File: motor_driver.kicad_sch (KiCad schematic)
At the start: 8 parts, among them J3 Conn_01x06, J4 Conn_01x06, U10 TB6612FNG

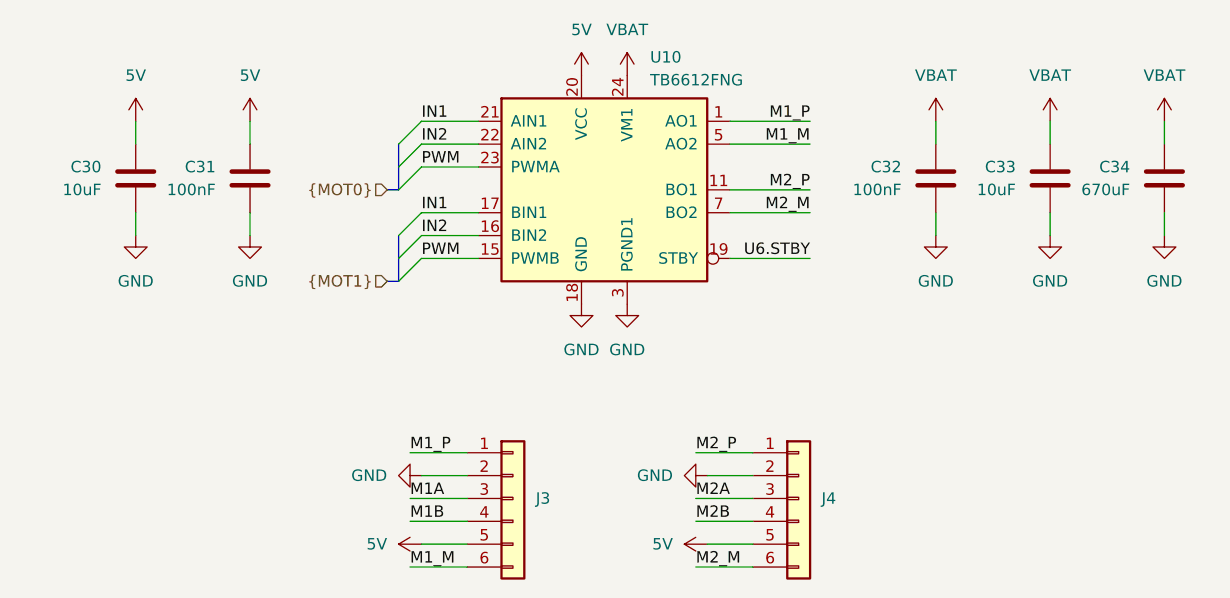
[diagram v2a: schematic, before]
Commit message: Follow DC-DC typical application
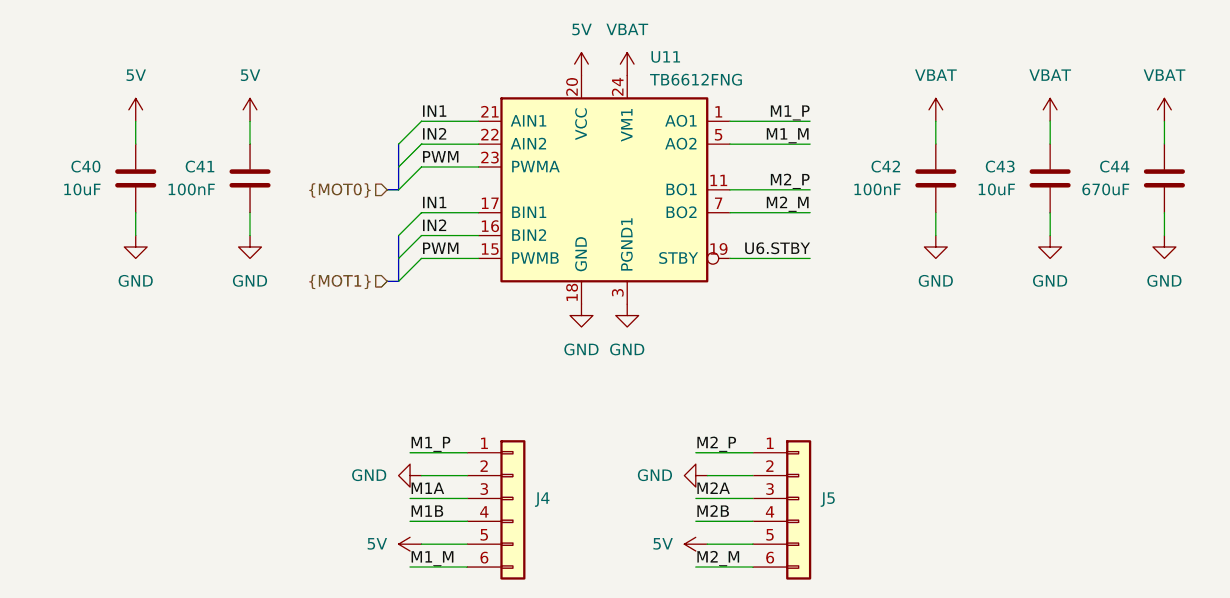
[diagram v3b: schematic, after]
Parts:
- renumbered C30 to C40, C31 to C41, C32 to C42, C33 to C43, C34 to C44, J3 to J4, J4 to J5, U10 to U11
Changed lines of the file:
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@@
 		(dnp no)
 		(fields_autoplaced yes)
-		(property "Reference" "#PWR0103"
+		(property "Reference" "#PWR0134"
 			(at 209.55 83.82 0)
 			(effects
@@
 			(project "Tumbler2_Redesign"
 				(path "/f3fd8d79-9d35-4c04-811e-2697a2740958/f393b342-ddad-47d4-8b4e-f21b64e15add"
-					(reference "#PWR0103")
+					(reference "#PWR0134")
 					(unit 1)
 				)
@@
 		(dnp no)
 		(fields_autoplaced yes)
-		(property "Reference" "#PWR0112"
+		(property "Reference" "#PWR0143"
 			(at 152.4 119.38 0)
 			(effects
@@
 			(project "Tumbler2_Redesign"
 				(path "/f3fd8d79-9d35-4c04-811e-2697a2740958/f393b342-ddad-47d4-8b4e-f21b64e15add"
-					(reference "#PWR0112")
+					(reference "#PWR0143")
 					(unit 1)
 				)
@@
 		(dnp no)
 		(fields_autoplaced yes)
-		(property "Reference" "#PWR098"
+		(property "Reference" "#PWR0129"
 			(at 149.86 78.74 0)
 			(effects
@@
 			(project "Tumbler2_Redesign"
 				(path "/f3fd8d79-9d35-4c04-811e-2697a2740958/f393b342-ddad-47d4-8b4e-f21b64e15add"
-					(reference "#PWR098")
+					(reference "#PWR0129")
 					(unit 1)
 				)
@@
 		(dnp no)
 		(fields_autoplaced yes)
-		(property "Reference" "#PWR099"
+		(property "Reference" "#PWR0130"
 			(at 95.25 83.82 0)
 			(effects
@@
 			(project "Tumbler2_Redesign"
 				(path "/f3fd8d79-9d35-4c04-811e-2697a2740958/f393b342-ddad-47d4-8b4e-f21b64e15add"
-					(reference "#PWR099")
+					(reference "#PWR0130")
 					(unit 1)
 				)
@@
 		(dnp no)
 		(fields_autoplaced yes)
-		(property "Reference" "#PWR0113"
+		(property "Reference" "#PWR0144"
 			(at 130.81 127 0)
 			(effects
@@
 			(project "Tumbler2_Redesign"
 				(path "/f3fd8d79-9d35-4c04-811e-2697a2740958/f393b342-ddad-47d4-8b4e-f21b64e15add"
-					(reference "#PWR0113")
+					(reference "#PWR0144")
 					(unit 1)
 				)
@@
 		(on_board yes)
 		(dnp no)
-		(property "Reference" "C31"
+		(property "Reference" "C41"
 			(at 104.14 85.0899 0)
 			(effects
@@
 			(project "Tumbler2_Redesign"
 				(path "/f3fd8d79-9d35-4c04-811e-2697a2740958/f393b342-ddad-47d4-8b4e-f21b64e15add"
-					(reference "C31")
+					(reference "C41")
 					(unit 1)
 				)
@@
 		(dnp no)
 		(fields_autoplaced yes)
-		(property "Reference" "#PWR0100"
+		(property "Reference" "#PWR0131"
 			(at 107.95 83.82 0)
 			(effects
@@
 			(project "Tumbler2_Redesign"
 				(path "/f3fd8d79-9d35-4c04-811e-2697a2740958/f393b342-ddad-47d4-8b4e-f21b64e15add"
-					(reference "#PWR0100")
+					(reference "#PWR0131")
 					(unit 1)
 				)
@@
 		(dnp no)
 		(fields_autoplaced yes)
-		(property "Reference" "#PWR0114"
+		(property "Reference" "#PWR0145"
 			(at 162.56 127 0)
 			(effects
@@
 			(project "Tumbler2_Redesign"
 				(path "/f3fd8d79-9d35-4c04-811e-2697a2740958/f393b342-ddad-47d4-8b4e-f21b64e15add"
-					(reference "#PWR0114")
+					(reference "#PWR0145")
 					(unit 1)
 				)
@@
 		(on_board yes)
 		(dnp no)
-		(property "Reference" "U10"
+		(property "Reference" "U11"
 			(at 152.4 72.898 0)
 			(effects
@@
 			(project "Tumbler2_Redesign"
 				(path "/f3fd8d79-9d35-4c04-811e-2697a2740958/f393b342-ddad-47d4-8b4e-f21b64e15add"
-					(reference "U10")
+					(reference "U11")
 					(unit 1)
 				)
@@
 		(on_board yes)
 		(dnp no)
-		(property "Reference" "C33"
+		(property "Reference" "C43"
 			(at 193.04 85.0899 0)
 			(effects
@@
 			(project "Tumbler2_Redesign"
 				(path "/f3fd8d79-9d35-4c04-811e-2697a2740958/f393b342-ddad-47d4-8b4e-f21b64e15add"
-					(reference "C33")
+					(reference "C43")
 					(unit 1)
 				)
@@
 		(dnp no)
 		(fields_autoplaced yes)
-		(property "Reference" "#PWR0105"
+		(property "Reference" "#PWR0136"
 			(at 107.95 99.06 0)
 			(effects
@@
 			(project "Tumbler2_Redesign"
 				(path "/f3fd8d79-9d35-4c04-811e-2697a2740958/f393b342-ddad-47d4-8b4e-f21b64e15add"
-					(reference "#PWR0105")
+					(reference "#PWR0136")
 					(unit 1)
 				)
@@
 		(dnp no)
 		(fields_autoplaced yes)
-		(property "Reference" "#PWR0109"
+		(property "Reference" "#PWR0140"
 			(at 144.78 106.68 0)
 			(effects
@@
 			(project "Tumbler2_Redesign"
 				(path "/f3fd8d79-9d35-4c04-811e-2697a2740958/f393b342-ddad-47d4-8b4e-f21b64e15add"
-					(reference "#PWR0109")
+					(reference "#PWR0140")
 					(unit 1)
 				)
@@
 		(dnp no)
 		(fields_autoplaced yes)
-		(property "Reference" "#PWR0111"
+		(property "Reference" "#PWR0142"
 			(at 120.65 119.38 0)
 			(effects
@@
 			(project "Tumbler2_Redesign"
 				(path "/f3fd8d79-9d35-4c04-811e-2697a2740958/f393b342-ddad-47d4-8b4e-f21b64e15add"
-					(reference "#PWR0111")
+					(reference "#PWR0142")
 					(unit 1)
 				)
@@
 		(dnp no)
 		(fields_autoplaced yes)
-		(property "Reference" "#PWR0101"
+		(property "Reference" "#PWR0132"
 			(at 184.15 83.82 0)
 			(effects
@@
 			(project "Tumbler2_Redesign"
 				(path "/f3fd8d79-9d35-4c04-811e-2697a2740958/f393b342-ddad-47d4-8b4e-f21b64e15add"
-					(reference "#PWR0101")
+					(reference "#PWR0132")
 					(unit 1)
 				)
@@
 		(dnp no)
 		(fields_autoplaced yes)
-		(property "Reference" "#PWR0108"
+		(property "Reference" "#PWR0139"
 			(at 209.55 99.06 0)
 			(effects
@@
 			(project "Tumbler2_Redesign"
 				(path "/f3fd8d79-9d35-4c04-811e-2697a2740958/f393b342-ddad-47d4-8b4e-f21b64e15add"
-					(reference "#PWR0108")
+					(reference "#PWR0139")
 					(unit 1)
 				)
@@
 		(on_board yes)
 		(dnp no)
-		(property "Reference" "C34"
+		(property "Reference" "C44"
 			(at 205.74 85.0899 0)
 			(effects
@@
 			(project "Tumbler2_Redesign"
 				(path "/f3fd8d79-9d35-4c04-811e-2697a2740958/f393b342-ddad-47d4-8b4e-f21b64e15add"
-					(reference "C34")
+					(reference "C44")
 					(unit 1)
 				)
@@
 		(dnp no)
 		(fields_autoplaced yes)
-		(property "Reference" "#PWR0107"
+		(property "Reference" "#PWR0138"
 			(at 196.85 99.06 0)
 			(effects
@@
 			(project "Tumbler2_Redesign"
 				(path "/f3fd8d79-9d35-4c04-811e-2697a2740958/f393b342-ddad-47d4-8b4e-f21b64e15add"
-					(reference "#PWR0107")
+					(reference "#PWR0138")
 					(unit 1)
 				)
@@
 		(on_board yes)
 		(dnp no)
-		(property "Reference" "J4"
+		(property "Reference" "J5"
 			(at 171.45 121.9199 0)
 			(effects
@@
 			(project "Tumbler2_Redesign"
 				(path "/f3fd8d79-9d35-4c04-811e-2697a2740958/f393b342-ddad-47d4-8b4e-f21b64e15add"
-					(reference "J4")
+					(reference "J5")
 					(unit 1)
 				)
@@
 		(dnp no)
 		(fields_autoplaced yes)
-		(property "Reference" "#PWR0106"
+		(property "Reference" "#PWR0137"
 			(at 184.15 99.06 0)
 			(effects
@@
 			(project "Tumbler2_Redesign"
 				(path "/f3fd8d79-9d35-4c04-811e-2697a2740958/f393b342-ddad-47d4-8b4e-f21b64e15add"
-					(reference "#PWR0106")
+					(reference "#PWR0137")
 					(unit 1)
 				)
@@
 		(dnp no)
 		(fields_autoplaced yes)
-		(property "Reference" "#PWR097"
+		(property "Reference" "#PWR0128"
 			(at 144.78 78.74 0)
 			(effects
@@
 			(project "Tumbler2_Redesign"
 				(path "/f3fd8d79-9d35-4c04-811e-2697a2740958/f393b342-ddad-47d4-8b4e-f21b64e15add"
-					(reference "#PWR097")
+					(reference "#PWR0128")
 					(unit 1)
 				)
@@
 		(on_board yes)
 		(dnp no)
-		(property "Reference" "J3"
+		(property "Reference" "J4"
 			(at 139.7 121.9199 0)
 			(effects
@@
 			(project "Tumbler2_Redesign"
 				(path "/f3fd8d79-9d35-4c04-811e-2697a2740958/f393b342-ddad-47d4-8b4e-f21b64e15add"
-					(reference "J3")
+					(reference "J4")
 					(unit 1)
 				)
@@
 		(on_board yes)
 		(dnp no)
-		(property "Reference" "C32"
+		(property "Reference" "C42"
 			(at 180.34 85.0899 0)
 			(effects
@@
 			(project "Tumbler2_Redesign"
 				(path "/f3fd8d79-9d35-4c04-811e-2697a2740958/f393b342-ddad-47d4-8b4e-f21b64e15add"
-					(reference "C32")
+					(reference "C42")
 					(unit 1)
 				)
@@
 		(dnp no)
 		(fields_autoplaced yes)
-		(property "Reference" "#PWR0104"
+		(property "Reference" "#PWR0135"
 			(at 95.25 99.06 0)
 			(effects
@@
 			(project "Tumbler2_Redesign"
 				(path "/f3fd8d79-9d35-4c04-811e-2697a2740958/f393b342-ddad-47d4-8b4e-f21b64e15add"
-					(reference "#PWR0104")
+					(reference "#PWR0135")
 					(unit 1)
 				)
@@
 		(dnp no)
 		(fields_autoplaced yes)
-		(property "Reference" "#PWR0102"
+		(property "Reference" "#PWR0133"
 			(at 196.85 83.82 0)
 			(effects
@@
 			(project "Tumbler2_Redesign"
 				(path "/f3fd8d79-9d35-4c04-811e-2697a2740958/f393b342-ddad-47d4-8b4e-f21b64e15add"
-					(reference "#PWR0102")
+					(reference "#PWR0133")
 					(unit 1)
 				)
@@
 		(dnp no)
 		(fields_autoplaced yes)
-		(property "Reference" "#PWR0110"
+		(property "Reference" "#PWR0141"
 			(at 149.86 106.68 0)
 			(effects
@@
 			(project "Tumbler2_Redesign"
 				(path "/f3fd8d79-9d35-4c04-811e-2697a2740958/f393b342-ddad-47d4-8b4e-f21b64e15add"
-					(reference "#PWR0110")
+					(reference "#PWR0141")
 					(unit 1)
 				)
@@
 		(on_board yes)
 		(dnp no)
-		(property "Reference" "C30"
+		(property "Reference" "C40"
 			(at 91.44 85.0899 0)
 			(effects
@@
 			(project "Tumbler2_Redesign"
 				(path "/f3fd8d79-9d35-4c04-811e-2697a2740958/f393b342-ddad-47d4-8b4e-f21b64e15add"
-					(reference "C30")
-					(unit 1)
-				)
+					(reference "C40")
+					(unit 1)
+				)

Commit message: Add test points
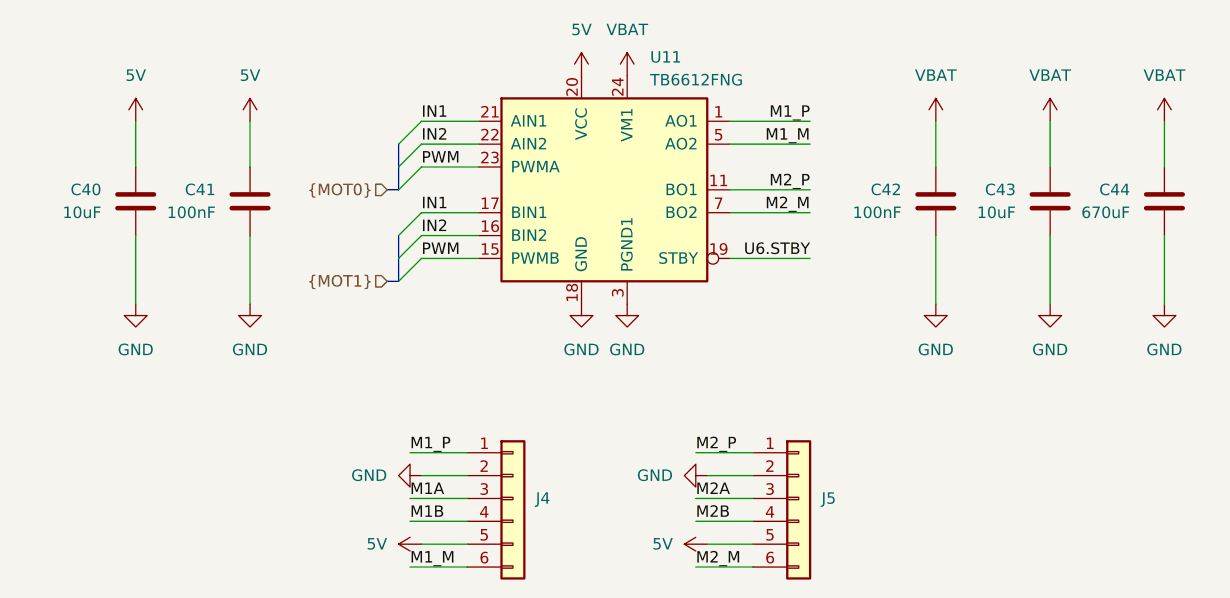
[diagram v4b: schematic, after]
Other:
- moved on the sheet: C40, C41, C42, C43, C44

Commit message: Assign footprints
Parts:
- C40, C43: footprint (none) -> Capacitor_SMD:C_0603_1608Metric_Pad1.08x0.95mm_HandSolder
- C41, C42: footprint (none) -> Capacitor_SMD:C_0402_1005Metric_Pad0.74x0.62mm_HandSolder
- C44: footprint (none) -> Capacitor_SMD:C_0805_2012Metric_Pad1.18x1.45mm_HandSolder
- J4, J5: footprint (none) -> Connector_PinHeader_2.54mm:PinHeader_1x06_P2.54mm_Vertical
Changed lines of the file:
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@@
 			)
 		)
-		(property "Footprint" ""
+		(property "Footprint" "Capacitor_SMD:C_0402_1005Metric_Pad0.74x0.62mm_HandSolder"
 			(at 106.9848 92.71 0)
 			(effects
@@
 			)
 		)
-		(property "Footprint" ""
+		(property "Footprint" "Capacitor_SMD:C_0603_1608Metric_Pad1.08x0.95mm_HandSolder"
 			(at 195.8848 92.71 0)
 			(effects
@@
 			)
 		)
-		(property "Footprint" ""
+		(property "Footprint" "Capacitor_SMD:C_0805_2012Metric_Pad1.18x1.45mm_HandSolder"
 			(at 208.5848 92.71 0)
 			(effects
@@
 			)
 		)
-		(property "Footprint" ""
+		(property "Footprint" "Connector_PinHeader_2.54mm:PinHeader_1x06_P2.54mm_Vertical"
 			(at 168.91 121.92 0)
 			(effects
@@
 			)
 		)
-		(property "Footprint" ""
+		(property "Footprint" "Connector_PinHeader_2.54mm:PinHeader_1x06_P2.54mm_Vertical"
 			(at 137.16 121.92 0)
 			(effects
@@
 			)
 		)
-		(property "Footprint" ""
+		(property "Footprint" "Capacitor_SMD:C_0402_1005Metric_Pad0.74x0.62mm_HandSolder"
 			(at 183.1848 92.71 0)
 			(effects
@@
 			)
 		)
-		(property "Footprint" ""
+		(property "Footprint" "Capacitor_SMD:C_0603_1608Metric_Pad1.08x0.95mm_HandSolder"
 			(at 94.2848 92.71 0)
 			(effects

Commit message: Assign LCSC part numbers
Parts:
- U11: LCSC Part (none) -> C141517
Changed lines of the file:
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@@
+			)
+		)
+		(property "LCSC Part" "C141517"
+			(at 147.32 87.63 0)
+			(effects
+				(font
+					(size 1.27 1.27)
+				)
+				(hide yes)
 			)
 		)

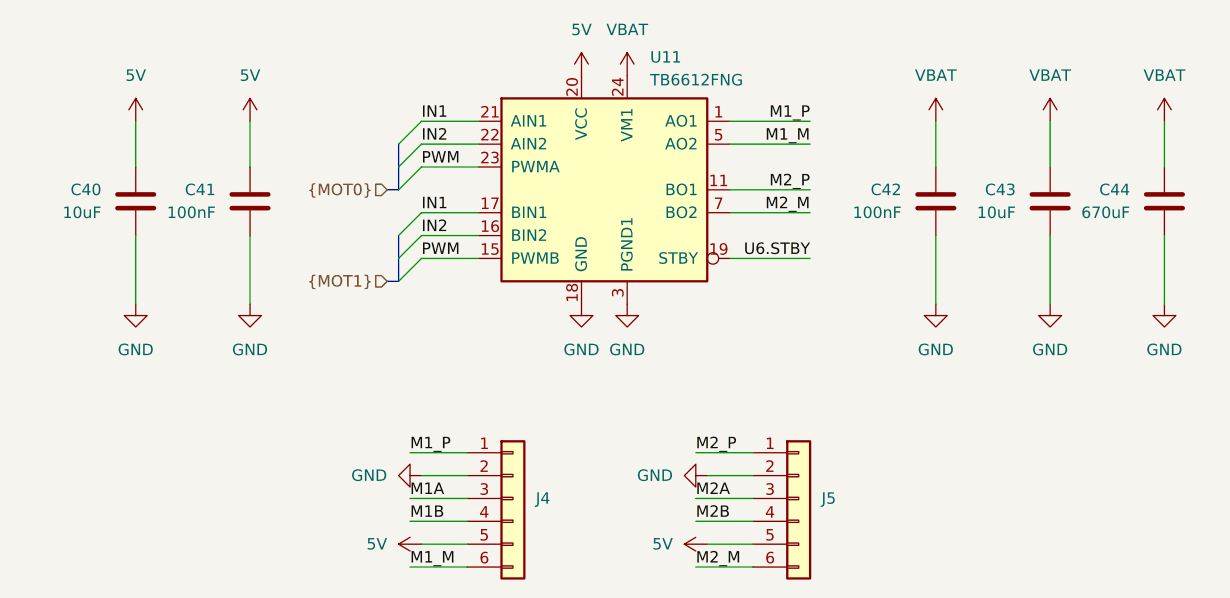
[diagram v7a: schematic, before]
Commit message: Use correct connector footprint
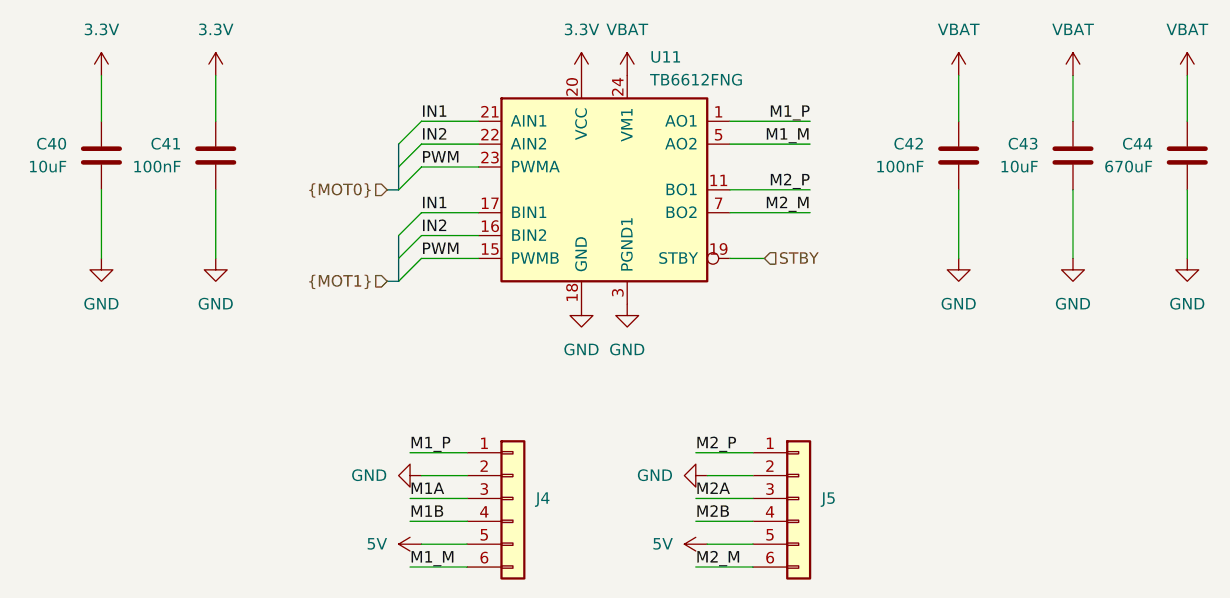
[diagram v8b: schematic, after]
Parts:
- J4, J5: footprint Connector_PinHeader_2.54mm:PinHeader_1x06_P2.54mm_Vertical -> Connector_JST:JST_PH_S6B-PH-SM4-TB_1x06-1MP_P2.00mm_Horizontal
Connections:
- net 5V: no longer C40.1, C41.1, U11.20 (VCC)
- net U6.STBY renamed STBY
- new net 3.3V: C40.1, C41.1, U11.20 (VCC)
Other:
- moved on the sheet: C40, C41, C42, C43, C44
